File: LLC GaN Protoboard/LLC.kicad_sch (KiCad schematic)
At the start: 5 parts, among them IC1 FAN73912AMX, IC2 BZX84-C5V6,215, IC3 BZX84-C5V6,215, Q1 CID10N65E3, Q2 CID10N65E3

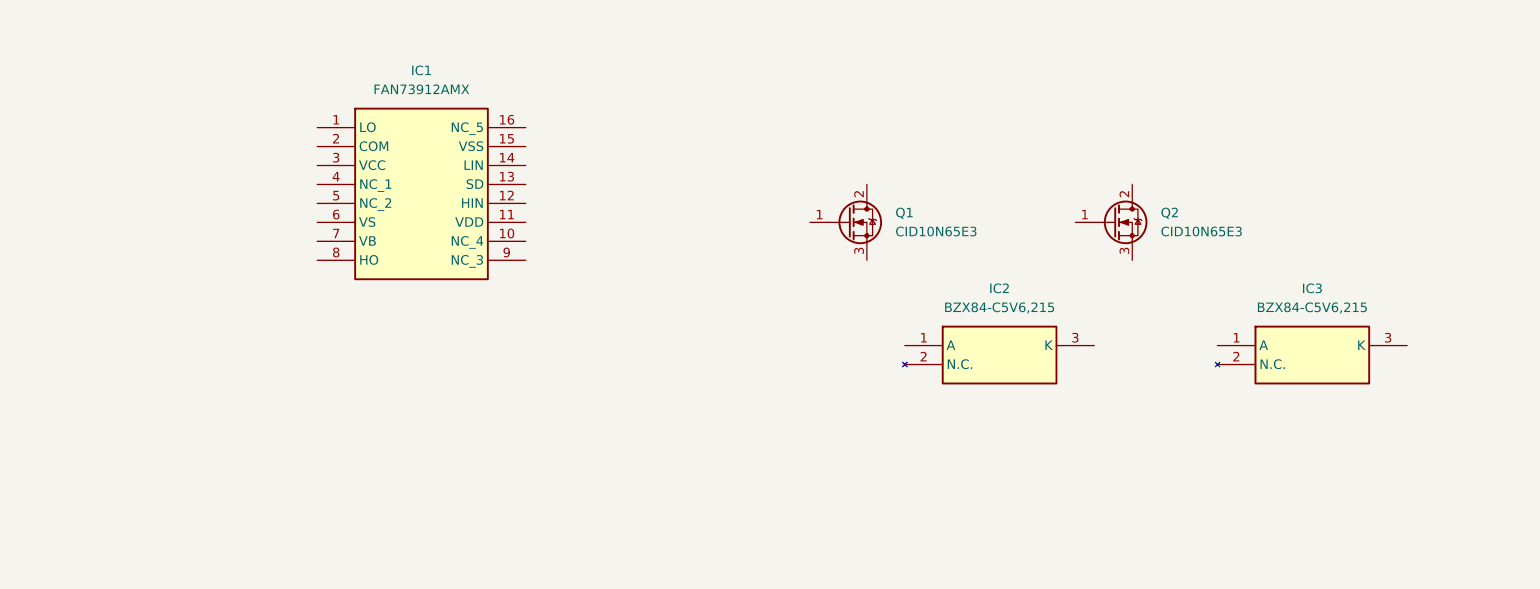
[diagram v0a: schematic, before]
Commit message: Added more calculations
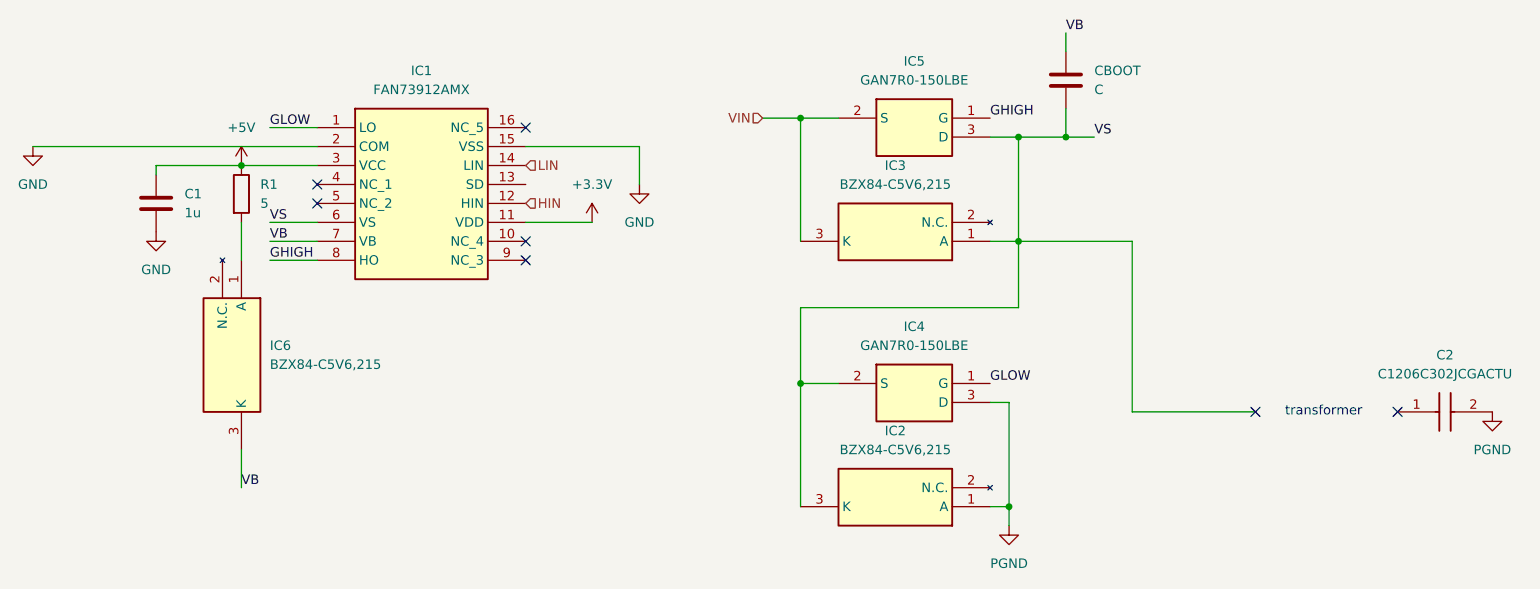
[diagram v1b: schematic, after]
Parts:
- removed Q1, Q2: CID10N65E3, Package_TO_SOT_SMD:TO-252-2, symbol Transistor_FET:QM6006D
- added C1: 1u, symbol Device:C
- added C2: C1206C302JCGACTU, C1206, symbol C1206C302JCGACTU:C1206C302JCGACTU
- added CBOOT: C, symbol Device:C
- added IC4, IC5: GAN7R0-150LBE, GAN7R0150LBE, symbol GAN7R0-150LBE:GAN7R0-150LBE
- added IC6: BZX84-C5V6,215, SOT95P230X110-3N, symbol BZX84-C5V6_215:BZX84-C5V6,215
- added R1: 5, symbol Device:R
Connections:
- net VS: now reaches IC3.1 (A)
- net VS: now also IC1.6 (VS), IC2.3 (K), CBOOT.2, IC4.2 (S), IC5.3 (D)
- net VIN: now reaches IC3.3 (K)
- net VIN: now also IC5.2 (S)
- net PGND: now reaches IC2.1 (A)
- net PGND: now also C2.2, IC4.3 (D)
- net GLOW: now reaches IC1.1 (LO)
- net GLOW: now also IC4.1 (G)
- net +3.3V: now reaches IC1.11 (VDD)
- net HIN: now reaches IC1.12 (HIN)
- net LIN: now reaches IC1.14 (LIN)
- net GND: now reaches IC1.15 (VSS)
- net GND: now also IC1.2 (COM), C1.2
- net +5V: now reaches IC1.3 (VCC)
- net +5V: now also C1.1, R1.1
- net VB: now reaches IC1.7 (VB)
- net VB: now also CBOOT.1, IC6.3 (K)
- net GHIGH: now reaches IC1.8 (HO)
- net GHIGH: now also IC5.1 (G)
- new net: IC6.1 (A), R1.2
- no-connect marks 0 -> 7
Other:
- note added: "transformer"
- moved on the sheet: IC2, IC3

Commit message: Initial layout
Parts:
- removed CBOOT: C, symbol Device:C
- added C3: C1812C104KDRACTU, C1812C104KDRACTU:C1812, symbol C1812C104KDRACTU:C1812C104KDRACTU
- added CBOOT1: C, Capacitor_SMD:C_0603_1608Metric, symbol Device:C
- added D1, D2, D3, D4: ADS12B3-ASARH, ADS12B3-ASARH:ADS12B3ASARH, symbol ADS12B3-ASARH:ADS12B3-ASARH
- added R2: WSC25155R000FEA, WSC25155R000FEA:RESM6438X317N, symbol WSC25155R000FEA:WSC25155R000FEA
- added R3: CRA2512-FZ-R050ELF, CRA2512-FZ-R050ELF:RESC6434X90N, symbol CRA2512-FZ-R050ELF:CRA2512-FZ-R050ELF
- added TP1, TP2, TP3, TP4, TP5, TP6, TP7, TP8: 5019, 5019:5019, symbol 5019:5019
- C1: footprint (none) -> Capacitor_SMD:C_0603_1608Metric
- C2: footprint C1206 -> C1206C302JCGACTU:C1206
- IC1: footprint SOIC127P1032X264-16N -> FAN73912AMX:SOIC127P1032X264-16N
- IC2, IC3, IC6: footprint SOT95P230X110-3N -> BZX84-C5V6,215:SOT95P230X110-3N
- IC4, IC5: footprint GAN7R0150LBE -> GAN7R0-150LBE:GAN7R0150LBE
- R1: footprint (none) -> Resistor_SMD:R_2010_5025Metric
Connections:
- net PGND: now also IC4.2 (S); no longer IC4.3 (D)
- net VB: now also CBOOT1.1
- net VS: now also IC4.3 (D), IC5.2 (S), CBOOT1.2; no longer IC4.2 (S), IC5.3 (D)
- net at C2.1: now also TP4.1
- net VIN renamed IIN_LOW
- net IIN_LOW: now also IC5.3 (D), R3.1, TP1.1; no longer IC5.2 (S)
- new net: TP2.1, TP3.1
- new net: D1.2 (A), D3.1 (K), TP5.1
- new net: D2.2 (A), D4.1 (K), TP6.1
- new net GND_ISO: C3.2, D3.2 (A), D4.2 (A), R2.1
- new net IIN_HIGH: R3.2
- new net IOUT_HIGH: R2.2, TP8.1
- new net VOUT: C3.1, D1.1 (K), D2.1 (K), TP7.1
- no-connect marks 7 -> 5
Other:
- note added: "inverter"
- note added: "rectifier"
- note added: "secondary"
- note added: "tuning inductor"
- moved on the sheet: C1, C2, IC1, IC2, IC3, IC4, IC5, IC6, R1

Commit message: Edited layout
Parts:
- added C4: .1u, Capacitor_SMD:C_0603_1608Metric, symbol Device:C
- added C5: 2.2u, Capacitor_SMD:C_0603_1608Metric, symbol Device:C
- added C6, C7: 1u, Capacitor_SMD:C_0603_1608Metric, symbol Device:C
- added C8: 22u, Capacitor_SMD:C_0603_1608Metric, symbol Device:C
- added D5: ADS12B3-ASARH, ADS12B3-ASARH:ADS12B3ASARH, symbol ADS12B3-ASARH:ADS12B3-ASARH
- added L1: SRR1260-150M, IND_BOURNS_SRR1260, symbol 2026-07-13_06-36-12:SRR1260-150M
- added R4: 118k, Resistor_SMD:R_2010_5025Metric, symbol Device:R
- added R5: 22.1k, Resistor_SMD:R_2010_5025Metric, symbol Device:R
- added R6: R, symbol Device:R
- added TP10, TP11, TP12, TP13, TP14, TP9: 5019, 5019:5019, symbol 5019:5019
- added U1: PLMR54410DBVR, U_SOT-23_TEX, symbol 2026-07-11_06-22-39:PLMR54410DBVR
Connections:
- net +5V: now also C8.1, L1.1, R4.1, TP10.1
- net GHIGH: now also TP13.1
- net GLOW: now also TP12.1
- net GND: now also C5.2, C8.2, R5.2, R6.1, TP11.1, U1.2 (GND)
- net IIN_HIGH: now also D5.2 (A)
- net IIN_LOW: now also C6.2; no longer TP1.1
- net PGND: now also C7.1, R6.2
- net VS: now also TP1.1, C6.1, C7.2, TP14.1
- new net: C4.2, L1.2, TP9.1, U1.6 (SW)
- new net: C4.1, U1.1 (CB)
- new net FB: R4.2, R5.1, U1.3 (FB)
- new net VIN_RECT: C5.1, D5.1 (K), U1.4 (EN), U1.5 (VIN)
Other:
- moved on the sheet: C2, CBOOT1, IC1, IC2, IC3, IC4, IC5, R3, TP1, TP2, TP3, TP4

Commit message: Finished schematic
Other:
- note added: "buck"
- moved on the sheet: C2, C4, C5, C8, D5, L1, R4, R5, R6, TP10, TP11, TP4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

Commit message: Edited schematic
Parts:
- added TP15, TP16, TP17: 5019, 5019:5019, symbol 5019:5019
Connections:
- net IIN_HIGH: now also TP16.1
- net IIN_LOW: now also TP15.1
- net PGND: now also TP17.1

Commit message: first route
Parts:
- removed TP12, TP13: 5019, 5019:5019, symbol 5019:5019
- added R21, R22: 1, Resistor_SMD:R_0603_1608Metric_Pad0.98x0.95mm_HandSolder, symbol Device:R
- L1: footprint IND_BOURNS_SRR1260 -> SRR1260-150M:SRR1260-150M
- R1, R4, R5: footprint Resistor_SMD:R_2010_5025Metric -> Resistor_SMD:R_0603_1608Metric_Pad0.98x0.95mm_HandSolder
- R6: footprint (none) -> Resistor_SMD:R_0603_1608Metric_Pad0.98x0.95mm_HandSolder
- U1: footprint U_SOT-23_TEX -> (none)
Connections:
- net GHIGH: now also R21.2; no longer IC5.1 (G)
- net GLOW: now also R22.2; no longer IC4.1 (G)
- new net: IC4.1 (G), R22.1
- new net: IC5.1 (G), R21.1
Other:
- moved on the sheet: TP1

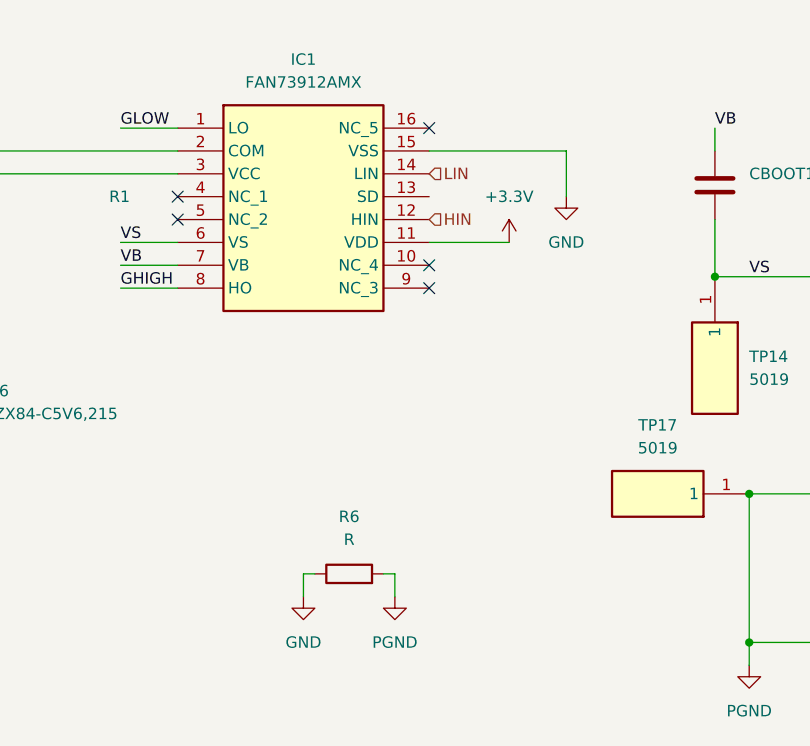
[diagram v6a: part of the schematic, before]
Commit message: Initial primary side layout
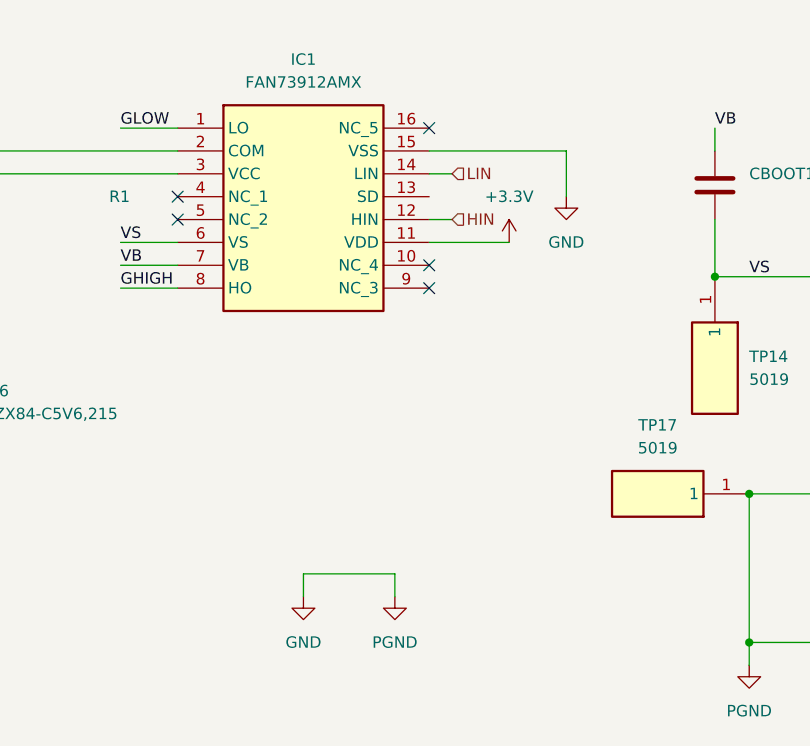
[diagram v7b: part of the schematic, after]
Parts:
- removed R6: R, Resistor_SMD:R_0603_1608Metric_Pad0.98x0.95mm_HandSolder, symbol Device:R
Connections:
- net PGND is gone; now on net GND: C2.2, C7.1, IC2.1 (A), IC4.2 (S), TP17.1
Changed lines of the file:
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@@
-	(wire
-		(pts
-			(xy 101.6 86.36) (xy 102.87 86.36)
-		)
-		(stroke
-			(width 0)
-			(type default)
-		)
-	)
 	(wire
 		(pts
@@
 	(wire
 		(pts
+			(xy 109.22 46.99) (xy 106.68 46.99)
+		)
+		(stroke
+			(width 0)
+			(type default)
+		)
+	)
+	(wire
+		(pts
 			(xy 215.9 147.32) (xy 220.98 147.32)
 		)
@@
 	(wire
 		(pts
-			(xy 92.71 86.36) (xy 93.98 86.36)
-		)
-		(stroke
-			(width 0)
-			(type default)
-		)
-	)
-	(wire
-		(pts
 			(xy 86.36 138.43) (xy 86.36 156.21)
 		)
@@
 	(wire
 		(pts
+			(xy 92.71 86.36) (xy 102.87 86.36)
+		)
+		(stroke
+			(width 0)
+			(type default)
+		)
+	)
+	(wire
+		(pts
 			(xy 46.99 171.45) (xy 58.42 171.45)
 		)
@@
 		(pts
 			(xy 220.98 147.32) (xy 220.98 148.59)
+		)
+		(stroke
+			(width 0)
+			(type default)
+		)
+	)
+	(wire
+		(pts
+			(xy 109.22 41.91) (xy 106.68 41.91)
 		)
 		(stroke
@@
 	(hierarchical_label "HIN"
 		(shape input)
-		(at 106.68 46.99 0)
+		(at 109.22 46.99 0)
 		(effects
 			(font
@@
 	(hierarchical_label "LIN"
 		(shape input)
-		(at 106.68 41.91 0)
+		(at 109.22 41.91 0)
 		(effects
 			(font
@@
 					(unit 1)
 				)
-			)
-		)
-	)
-	(symbol
-		(lib_id "Device:R")
-		(at 97.79 86.36 90)
-		(unit 1)
-		(body_style 1)
-		(exclude_from_sim no)
-		(in_bom yes)
-		(on_board yes)
-		(in_pos_files yes)
-		(dnp no)
-		(fields_autoplaced yes)
-		(property "Reference" "R6"
-			(at 97.79 80.01 90)
-			(show_name no)
-			(do_not_autoplace no)
-			(effects
-				(font
-					(size 1.27 1.27)
-				)
-			)
-		)
-		(property "Value" "R"
-			(at 97.79 82.55 90)
-			(show_name no)
-			(do_not_autoplace no)
-			(effects
-				(font
-					(size 1.27 1.27)
-				)
-			)
-		)
-		(property "Footprint" "Resistor_SMD:R_0603_1608Metric_Pad0.98x0.95mm_HandSolder"
-			(at 97.79 88.138 90)
-			(hide yes)
-			(show_name no)
-			(do_not_autoplace no)
-			(effects
-				(font
-					(size 1.27 1.27)
-				)
-			)
-		)
-		(property "Datasheet" ""
-			(at 97.79 86.36 0)
-			(hide yes)
-			(show_name no)
-			(do_not_autoplace no)
-			(effects
-				(font
-					(size 1.27 1.27)
-				)
-			)
-		)
-		(property "Description" "Resistor"
-			(at 97.79 86.36 0)
-			(hide yes)
-			(show_name no)
-			(do_not_autoplace no)
-			(effects
-				(font
-					(size 1.27 1.27)
-				)
-			)
-		)
-		(pin "1"
-		)
-		(pin "2"
-		)
-		(instances
-			(project "LLC GaN Protoboard"
-				(path "/07813ae8-ed9f-4173-b5dd-dce781eafd3c/af6a3929-d855-42a5-9472-0d99d4fa635d"
-					(reference "R6")
-					(unit 1)
-				)

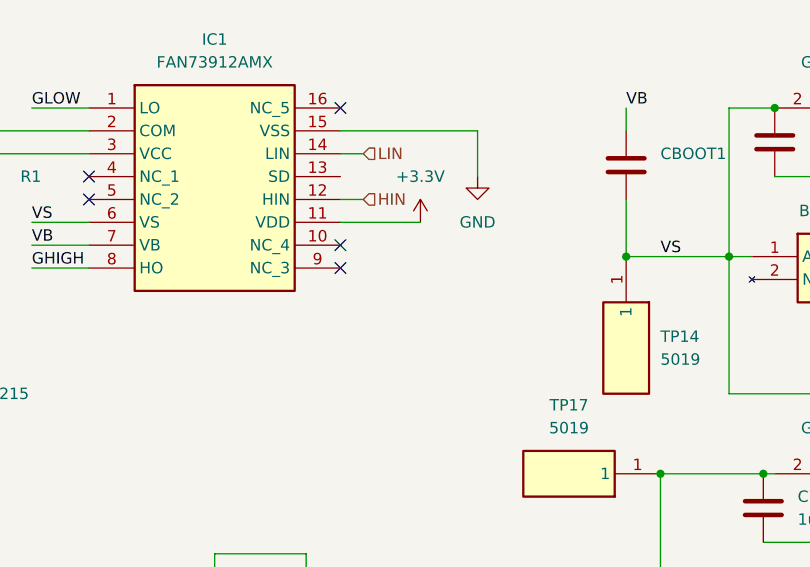
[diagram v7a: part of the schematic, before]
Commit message: Added open spots for soldering
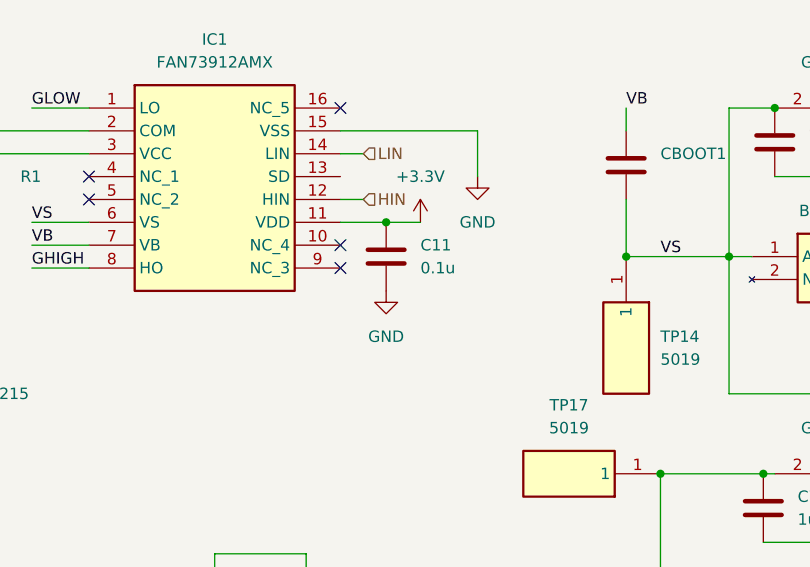
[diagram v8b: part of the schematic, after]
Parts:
- added C11: 0.1u, Capacitor_SMD:C_0603_1608Metric, symbol Device:C
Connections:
- net +3.3V: now also C11.1
- net GND: now also C11.2
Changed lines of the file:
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@@
 	)
 	(junction
-		(at 142.24 93.98)
+		(at 251.46 138.43)
 		(diameter 0)
 		(color 0 0 0 0)
 	)
 	(junction
-		(at 251.46 138.43)
+		(at 149.86 53.34)
 		(diameter 0)
 		(color 0 0 0 0)
 	)
 	(junction
-		(at 149.86 53.34)
+		(at 251.46 129.54)
 		(diameter 0)
 		(color 0 0 0 0)
 	)
 	(junction
-		(at 251.46 129.54)
+		(at 111.76 49.53)
 		(diameter 0)
 		(color 0 0 0 0)
@@
 	)
 	(junction
+		(at 142.24 93.98)
+		(diameter 0)
+		(color 0 0 0 0)
+	)
+	(junction
 		(at 176.53 39.37)
 		(diameter 0)
@@
 	(wire
 		(pts
+			(xy 111.76 49.53) (xy 115.57 49.53)
+		)
+		(stroke
+			(width 0)
+			(type default)
+		)
+	)
+	(wire
+		(pts
 			(xy 179.07 39.37) (xy 179.07 53.34)
 		)
@@
 	(wire
 		(pts
-			(xy 106.68 49.53) (xy 115.57 49.53)
+			(xy 106.68 49.53) (xy 111.76 49.53)
 		)
 		(stroke
@@
 	)
 	(symbol
+		(lib_id "power:GND")
+		(at 111.76 57.15 0)
+		(unit 1)
+		(body_style 1)
+		(exclude_from_sim no)
+		(in_bom yes)
+		(on_board yes)
+		(in_pos_files yes)
+		(dnp no)
+		(fields_autoplaced yes)
+		(property "Reference" "#PWR046"
+			(at 111.76 63.5 0)
+			(hide yes)
+			(show_name no)
+			(do_not_autoplace no)
+			(effects
+				(font
+					(size 1.27 1.27)
+				)
+			)
+		)
+		(property "Value" "GND"
+			(at 111.76 62.23 0)
+			(show_name no)
+			(do_not_autoplace no)
+			(effects
+				(font
+					(size 1.27 1.27)
+				)
+			)
+		)
+		(property "Footprint" ""
+			(at 111.76 57.15 0)
+			(hide yes)
+			(show_name no)
+			(do_not_autoplace no)
+			(effects
+				(font
+					(size 1.27 1.27)
+				)
+			)
+		)
+		(property "Datasheet" ""
+			(at 111.76 57.15 0)
+			(hide yes)
+			(show_name no)
+			(do_not_autoplace no)
+			(effects
+				(font
+					(size 1.27 1.27)
+				)
+			)
+		)
+		(property "Description" "Power symbol creates a global label with name \"GND\" , ground"
+			(at 111.76 57.15 0)
+			(hide yes)
+			(show_name no)
+			(do_not_autoplace no)
+			(effects
+				(font
+					(size 1.27 1.27)
+				)
+			)
+		)
+		(pin "1"
+		)
+		(instances
+			(project "LLC GaN Protoboard"
+				(path "/07813ae8-ed9f-4173-b5dd-dce781eafd3c/af6a3929-d855-42a5-9472-0d99d4fa635d"
+					(reference "#PWR046")
+					(unit 1)
+				)
+			)
+		)
+	)
+	(symbol
 		(lib_id "5019:5019")
 		(at 138.43 53.34 270)
@@
 					(unit 1)
 				)
+			)
+		)
+	)
+	(symbol
+		(lib_id "Device:C")
+		(at 111.76 53.34 0)
+		(unit 1)
+		(body_style 1)
+		(exclude_from_sim no)
+		(in_bom yes)
+		(on_board yes)
+		(in_pos_files yes)
+		(dnp no)
+		(fields_autoplaced yes)
+		(property "Reference" "C11"
+			(at 115.57 52.0699 0)
+			(show_name no)
+			(do_not_autoplace no)
+			(effects
+				(font
+					(size 1.27 1.27)
+				)
+				(justify left)
+			)
+		)
+		(property "Value" "0.1u"
+			(at 115.57 54.6099 0)
+			(show_name no)
+			(do_not_autoplace no)
+			(effects
+				(font
+					(size 1.27 1.27)
+				)
+				(justify left)
+			)
+		)
+		(property "Footprint" "Capacitor_SMD:C_0603_1608Metric"
+			(at 112.7252 57.15 0)
+			(hide yes)
+			(show_name no)
+			(do_not_autoplace no)
+			(effects
+				(font
+					(size 1.27 1.27)
+				)
+			)
+		)
+		(property "Datasheet" ""
+			(at 111.76 53.34 0)
+			(hide yes)
+			(show_name no)
+			(do_not_autoplace no)
+			(effects
+				(font
+					(size 1.27 1.27)
+				)
+			)
+		)
+		(property "Description" "Unpolarized capacitor"
+			(at 111.76 53.34 0)
+			(hide yes)
+			(show_name no)
+			(do_not_autoplace no)
+			(effects
+				(font
+					(size 1.27 1.27)
+				)
+			)
+		)
+		(pin "1"
+		)
+		(pin "2"
+		)
+		(instances
+			(project "LLC GaN Protoboard"
+				(path "/07813ae8-ed9f-4173-b5dd-dce781eafd3c/af6a3929-d855-42a5-9472-0d99d4fa635d"
+					(reference "C11")
+					(unit 1)
+				)
